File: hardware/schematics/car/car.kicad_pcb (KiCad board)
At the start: 12 copper layers, 53.3 x 107.8 mm, 22 parts, among them M1 Motor_Servo, Q1 PMOS, SW1 SW_SPST, SW2 SW_Push, SW3 SW_Push, U1 VL53L0CXV0DH1, U10 Mini-560, U11 JGA25-37x, U2 VL53L0CXV0DH1, U3 VL53L0CXV0DH1, U4 Pixy2, U6 TB6612FNG, U7 SparkFun OTOS, U9 Mini-360

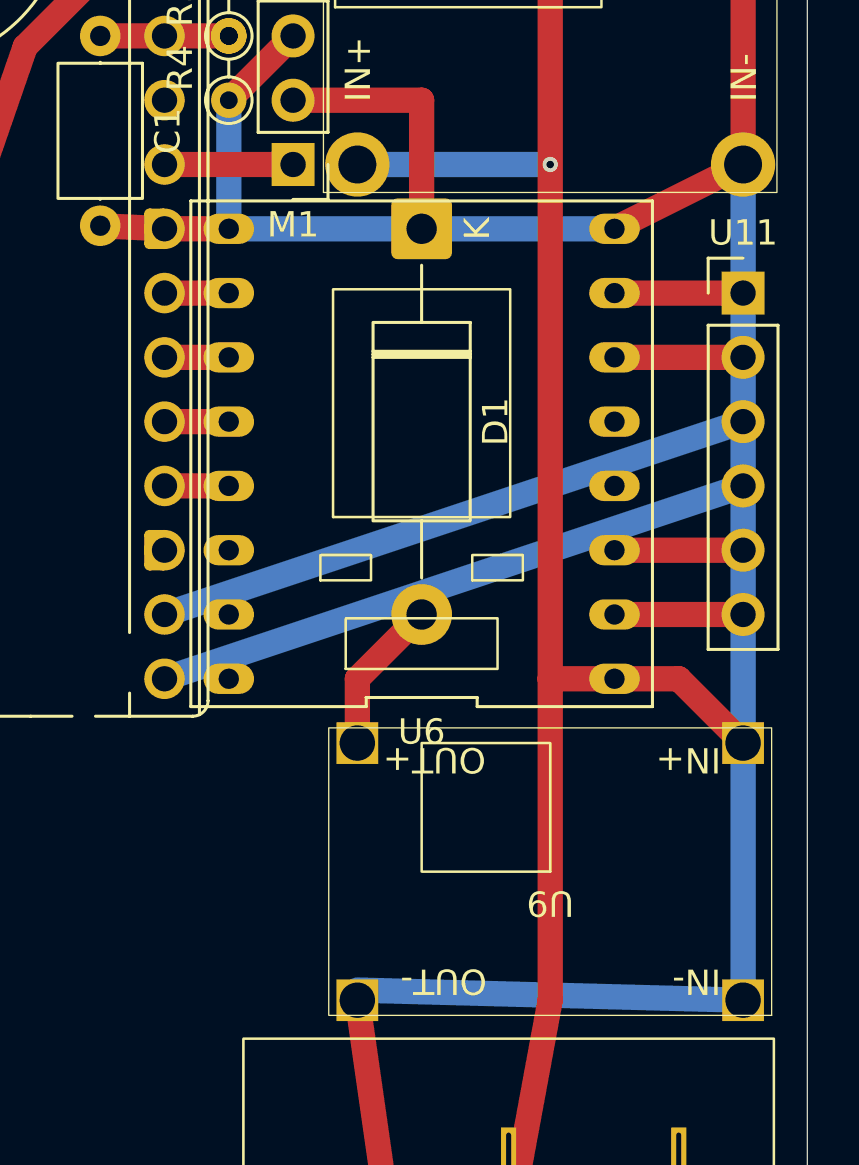
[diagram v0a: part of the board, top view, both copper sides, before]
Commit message: [Schematic] Move left by one motor connector.
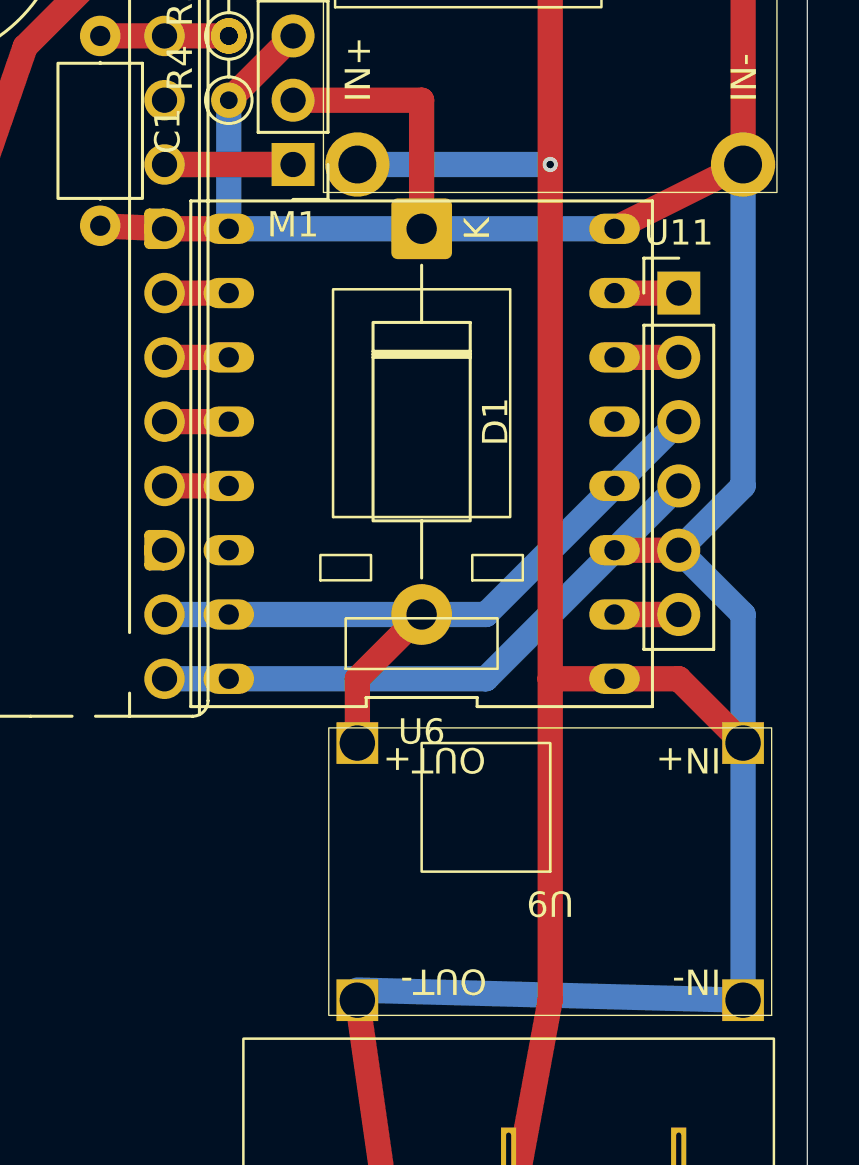
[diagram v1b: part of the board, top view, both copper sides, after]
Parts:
- moved U11 2.54 mm to (165.1, 48.3)
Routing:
- net Net-(U11-M2): track 5.08 -> 2.54 mm
- net Net-(U11-M1): track 5.08 -> 2.54 mm
- net +3.3V: track 91.3 -> 88.8 mm
- net Net-(A1-GPIO17): track 24.1 -> 23.5 mm
- net Net-(A1-GPIO16): track 24.1 -> 23.5 mm
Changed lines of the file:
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@@
 	(footprint "xlnc-foot:JGA25-37x_PinHeader_1x06_P2.54mm_Vertical"
 		(layer "F.Cu")
-		(at 167.64 48.26)
+		(at 165.1 48.26)
 		(descr "Through hole straight pin header, 1x06, 2.54mm pitch, single row")
 		(tags "Through hole pin header THT 1x06 2.54mm single row")
@@
 	)
 	(segment
+		(start 165.1 58.42)
+		(end 162.56 58.42)
+		(width 1)
+		(layer "F.Cu")
+		(net "GND")
+	)
+	(segment
 		(start 142.24 45.6)
 		(end 144.78 45.72)
@@
 	)
 	(segment
-		(start 167.64 58.42)
-		(end 162.56 58.42)
-		(width 1)
-		(layer "F.Cu")
-		(net "GND")
-	)
-	(segment
 		(start 167.64 43.18)
 		(end 162.56 45.72)
@@
 	)
 	(segment
-		(start 167.64 58.42)
+		(start 167.64 55.88)
 		(end 167.64 43.18)
+		(width 1)
+		(layer "B.Cu")
+		(net "GND")
+	)
+	(segment
+		(start 167.64 76.2)
+		(end 167.64 60.96)
+		(width 1)
+		(layer "B.Cu")
+		(net "GND")
+	)
+	(segment
+		(start 167.64 60.96)
+		(end 165.1 58.42)
 		(width 1)
 		(layer "B.Cu")
@@
 	)
 	(segment
+		(start 165.1 58.42)
+		(end 167.64 55.88)
+		(width 1)
+		(layer "B.Cu")
+		(net "GND")
+	)
+	(segment
 		(start 167.64 76.2)
 		(end 152.4 75.8)
@@
 		(start 162.56 45.72)
 		(end 147.32 45.72)
-		(width 1)
-		(layer "B.Cu")
-		(net "GND")
-	)
-	(segment
-		(start 167.64 76.2)
-		(end 167.64 58.42)
 		(width 1)
 		(layer "B.Cu")
@@
 	)
 	(segment
-		(start 167.64 50.8)
+		(start 165.1 50.8)
 		(end 162.56 50.8)
 		(width 1)
@@
 	)
 	(segment
-		(start 167.64 48.26)
+		(start 165.1 48.26)
 		(end 162.56 48.26)
 		(width 1)
@@
 	)
 	(segment
-		(start 167.64 60.96)
+		(start 165.1 60.96)
 		(end 162.56 60.96)
 		(width 1)
@@
 	)
 	(segment
-		(start 167.64 55.88)
-		(end 144.78 63.5)
+		(start 165.1 55.88)
+		(end 157.48 63.5)
 		(width 1)
 		(layer "B.Cu")
@@
 	)
 	(segment
-		(start 167.64 53.34)
+		(start 157.48 63.5)
+		(end 144.78 63.5)
+		(width 1)
+		(layer "B.Cu")
+		(net "Net-(A1-GPIO16)")
+	)
+	(segment
+		(start 165.1 53.34)
+		(end 157.48 60.96)
+		(width 1)
+		(layer "B.Cu")
+		(net "Net-(A1-GPIO17)")
+	)
+	(segment
+		(start 157.48 60.96)
 		(end 144.78 60.96)
 		(width 1)

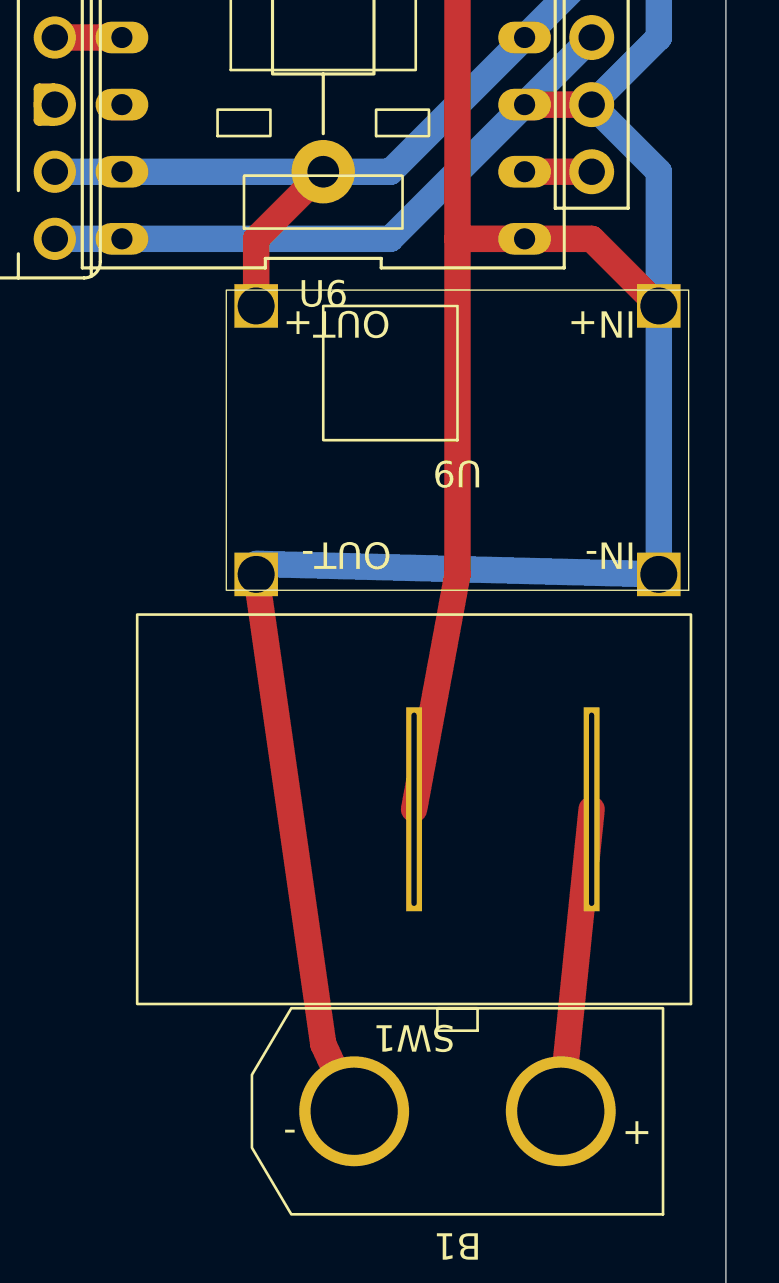
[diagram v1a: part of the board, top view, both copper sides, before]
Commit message: [Schematic] moved mini-360 to replace it and not clean the through holes.
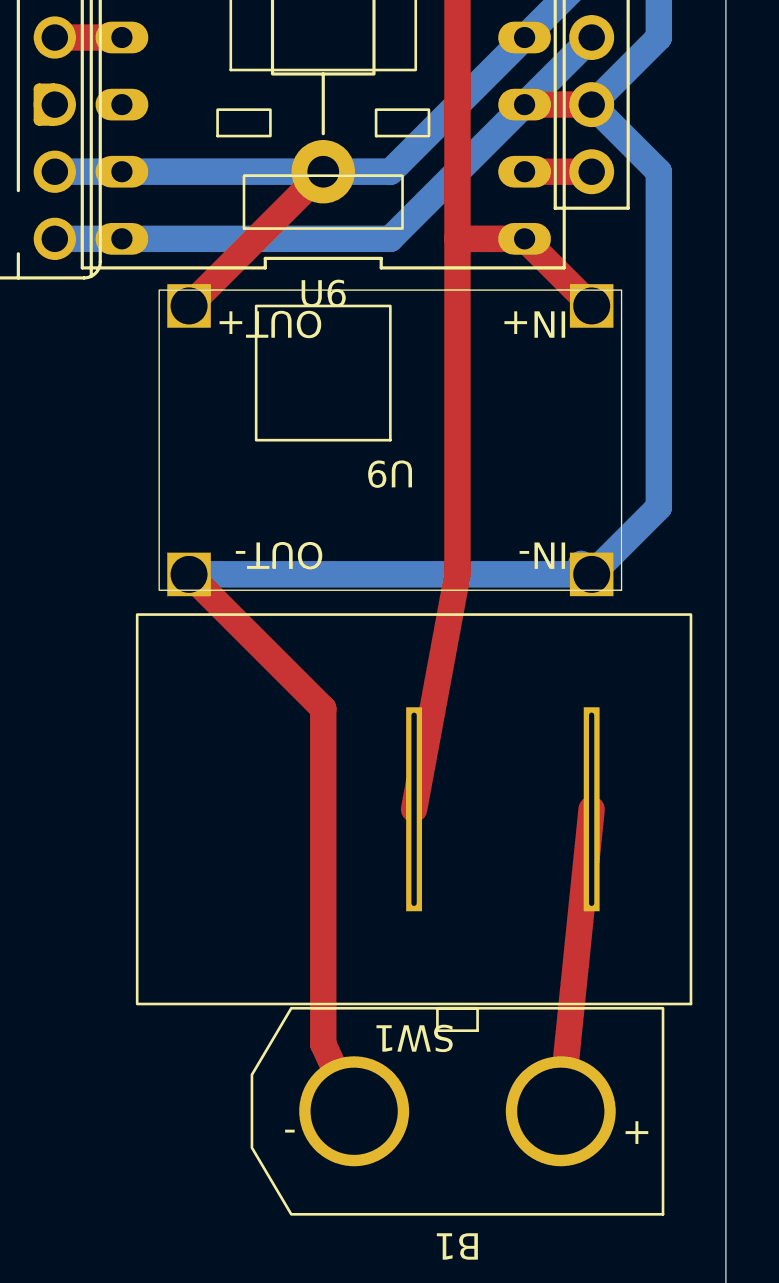
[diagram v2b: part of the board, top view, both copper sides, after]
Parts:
- moved U9 2.54 mm to (157.5, 71.1)
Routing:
- net GND: track 335.2 -> 338.8 mm
- net VBAT: track 78.7 -> 76.1 mm
- net +6V: track 6.13 -> 7.18 mm
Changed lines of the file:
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@@
 	(footprint "xlnc-foot:Buck_Mini-360_2.54mm"
 		(layer "F.Cu")
-		(at 160.02 71.12 180)
+		(at 157.48 71.12 180)
 		(property "Reference" "U9"
 			(at 0 -1.25 180)
@@
 	)
 	(segment
-		(start 156.11 96.52)
+		(start 154.94 81.28)
 		(end 154.94 93.98)
 		(width 1)
@@
 	)
 	(segment
-		(start 121.92 33.02)
-		(end 119.38 33.02)
+		(start 154.94 93.98)
+		(end 156.11 96.52)
 		(width 1)
 		(layer "F.Cu")
@@
 	)
 	(segment
-		(start 152.4 76.2)
-		(end 154.94 93.98)
+		(start 149.86 76.2)
+		(end 154.94 81.28)
+		(width 1)
+		(layer "F.Cu")
+		(net "GND")
+	)
+	(segment
+		(start 121.92 33.02)
+		(end 119.38 33.02)
 		(width 1)
 		(layer "F.Cu")
@@
 	)
 	(segment
-		(start 167.64 76.2)
-		(end 167.64 60.96)
+		(start 165.1 76.2)
+		(end 167.64 73.66)
 		(width 1)
 		(layer "B.Cu")
@@
 	)
 	(segment
-		(start 167.64 60.96)
-		(end 165.1 58.42)
+		(start 147.32 45.72)
+		(end 147.32 40.64)
 		(width 1)
 		(layer "B.Cu")
@@
 	)
 	(segment
-		(start 147.32 45.72)
-		(end 147.32 40.64)
+		(start 165.1 58.42)
+		(end 167.64 55.88)
 		(width 1)
 		(layer "B.Cu")
@@
 	)
 	(segment
-		(start 165.1 58.42)
-		(end 167.64 55.88)
+		(start 167.64 73.66)
+		(end 167.64 60.96)
 		(width 1)
 		(layer "B.Cu")
@@
 	)
 	(segment
-		(start 167.64 76.2)
-		(end 152.4 75.8)
+		(start 165.1 76.2)
+		(end 164.7 75.8)
+		(width 1)
+		(layer "B.Cu")
+		(net "GND")
+	)
+	(segment
+		(start 165.1 76.2)
+		(end 149.86 76.2)
 		(width 1)
 		(layer "B.Cu")
@@
 	)
 	(segment
+		(start 167.64 60.96)
+		(end 165.1 58.42)
+		(width 1)
+		(layer "B.Cu")
+		(net "GND")
+	)
+	(segment
 		(start 127 45.72)
 		(end 144.78 58.42)
@@
 	)
 	(segment
-		(start 160.02 63.5)
-		(end 165.1 63.5)
+		(start 158.3775 85.09)
+		(end 160.02 76.2)
 		(width 1)
 		(layer "F.Cu")
@@
 	)
 	(segment
-		(start 158.3775 85.09)
-		(end 160.02 76.2)
+		(start 165.1 66.04)
+		(end 162.56 63.5)
 		(width 1)
 		(layer "F.Cu")
@@
 	)
 	(segment
-		(start 160.02 35.56)
-		(end 147.32 35.56)
+		(start 162.56 63.5)
+		(end 160.02 63.5)
 		(width 1)
 		(layer "F.Cu")
@@
 	)
 	(segment
-		(start 167.64 66.04)
-		(end 165.1 63.5)
+		(start 160.02 35.56)
+		(end 147.32 35.56)
 		(width 1)
 		(layer "F.Cu")
@@
 	)
 	(segment
-		(start 152.4 66.04)
-		(end 152.4 63.5)
-		(width 1)
-		(layer "F.Cu")
-		(net "+6V")
-	)
-	(segment
-		(start 152.4 63.5)
+		(start 149.86 66.04)
 		(end 154.94 60.96)
 		(width 1)

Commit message: Add potential holes in perfboard
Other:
- board size 53.3 x 107.8 mm -> 63.5 x 107.8 mm
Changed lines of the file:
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@@
 	)
 	(gr_rect
-		(start 116.84 14.135)
-		(end 170.18 121.92)
+		(start 111.77 13.97)
+		(end 175.27 121.755)
 		(stroke
 			(width 0.05)
+			(type default)
+		)
+		(fill no)
+		(layer "Edge.Cuts")
+	)
+	(gr_circle
+		(center 114.3 20.32)
+		(end 116.84 20.32)
+		(stroke
+			(width 0.05)
+			(type default)
+		)
+		(fill no)
+		(layer "Edge.Cuts")
+	)
+	(gr_circle
+		(center 114.3 116.84)
+		(end 116.84 116.84)
+		(stroke
+			(width 0.05)
+			(type default)
+		)
+		(fill no)
+		(layer "Edge.Cuts")
+	)
+	(gr_circle
+		(center 172.72 20.32)
+		(end 170.18 20.32)
+		(stroke
+			(width 0.05)
+			(type default)
+		)
+		(fill no)
+		(layer "Edge.Cuts")
+	)
+	(gr_circle
+		(center 172.72 116.84)
+		(end 175.26 116.84)
+		(stroke
+			(width 0.05)

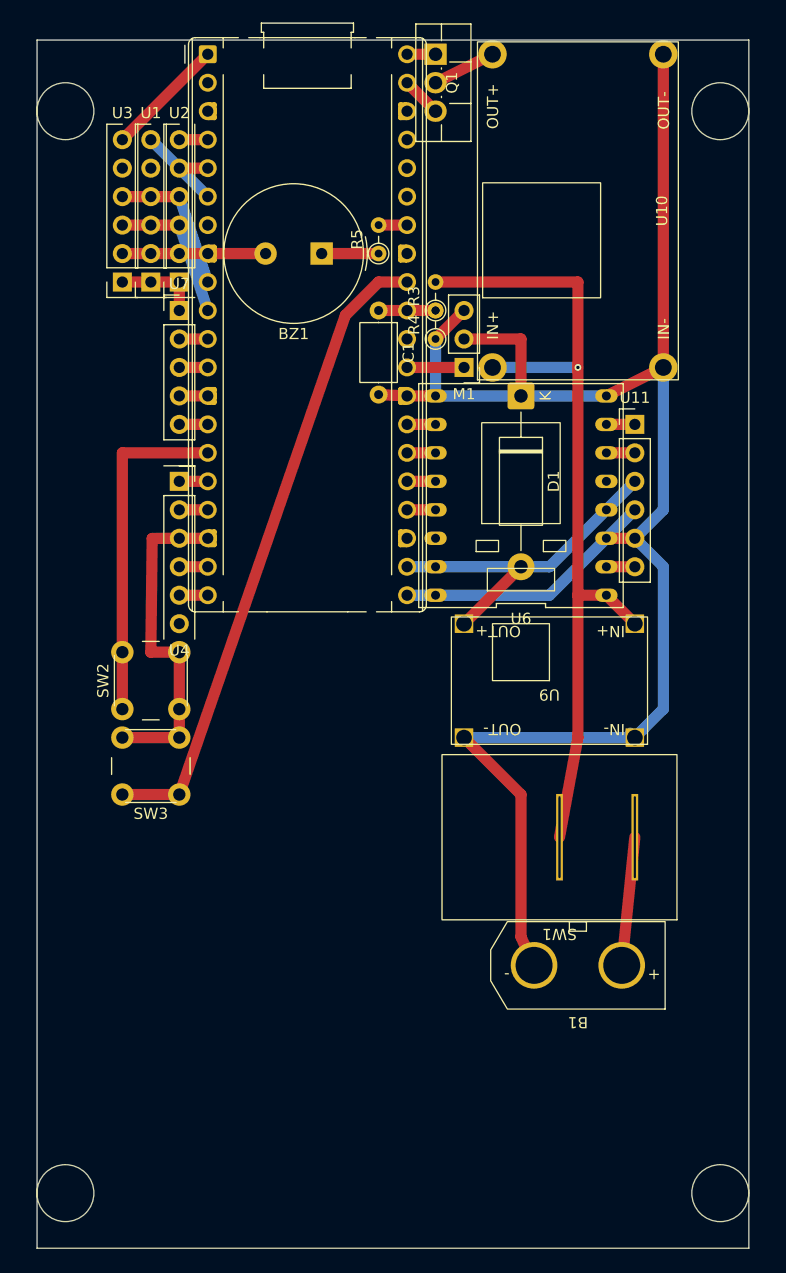
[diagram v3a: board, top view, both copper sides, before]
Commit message: [Schematic] PCB: Change holes and boundary to real. Add second pico(just visual)
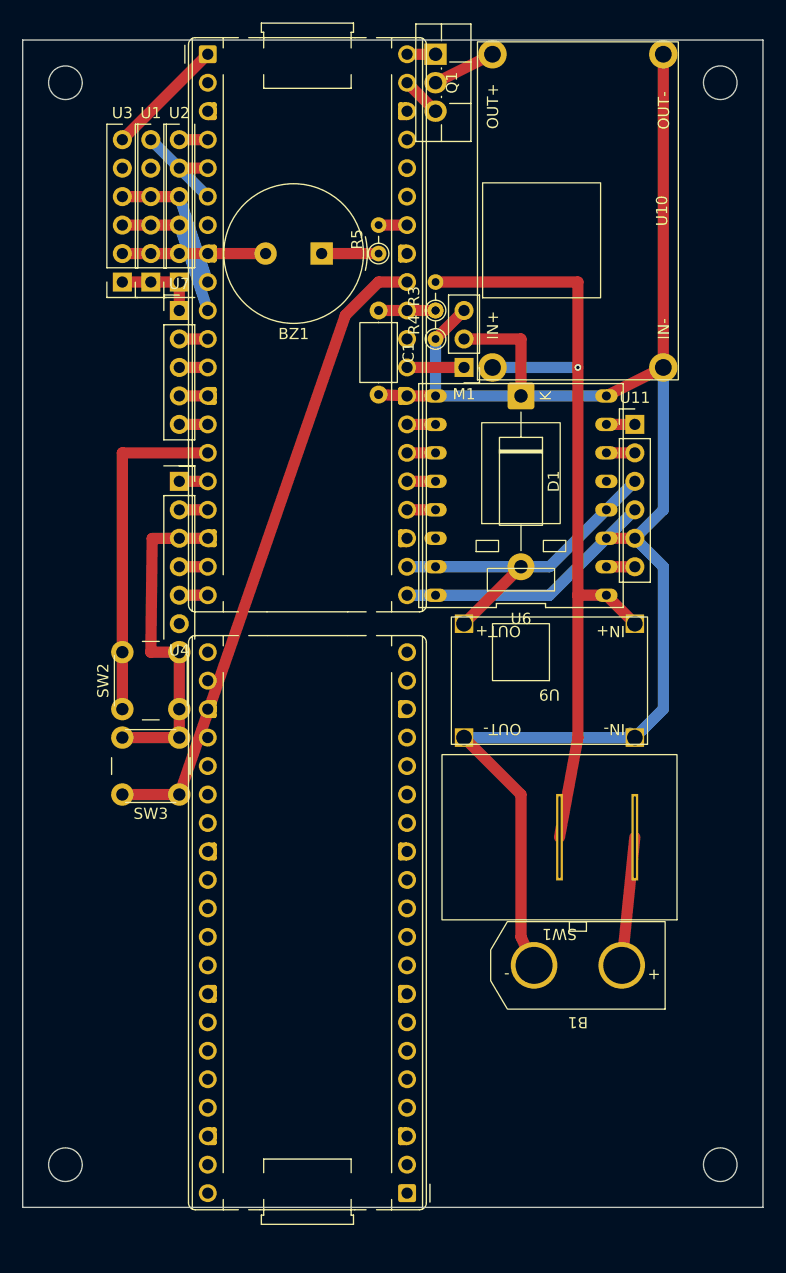
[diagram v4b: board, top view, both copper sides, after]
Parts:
- added A1: RaspberryPi_Pico2, Module:RaspberryPi_Pico_Common_THT, F.Cu at (144.8, 116.8)
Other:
- board size 63.5 x 107.8 mm -> 66 x 104.1 mm
